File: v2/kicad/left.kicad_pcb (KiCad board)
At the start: 2 copper layers, 158.5 x 120.3 mm, 66 parts

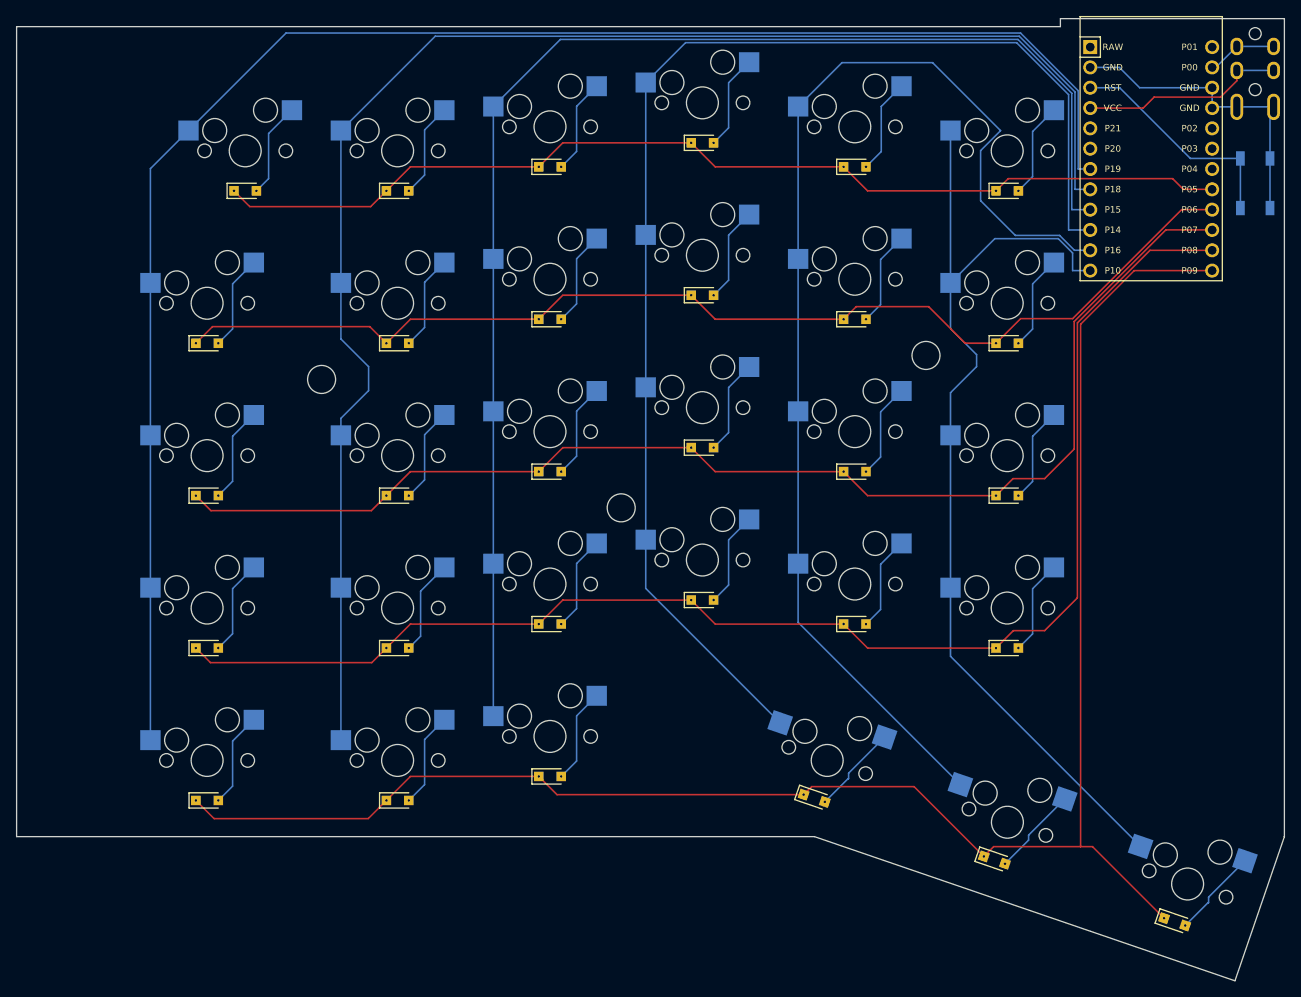
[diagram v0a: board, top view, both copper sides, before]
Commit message: Move backspace 1u to the left
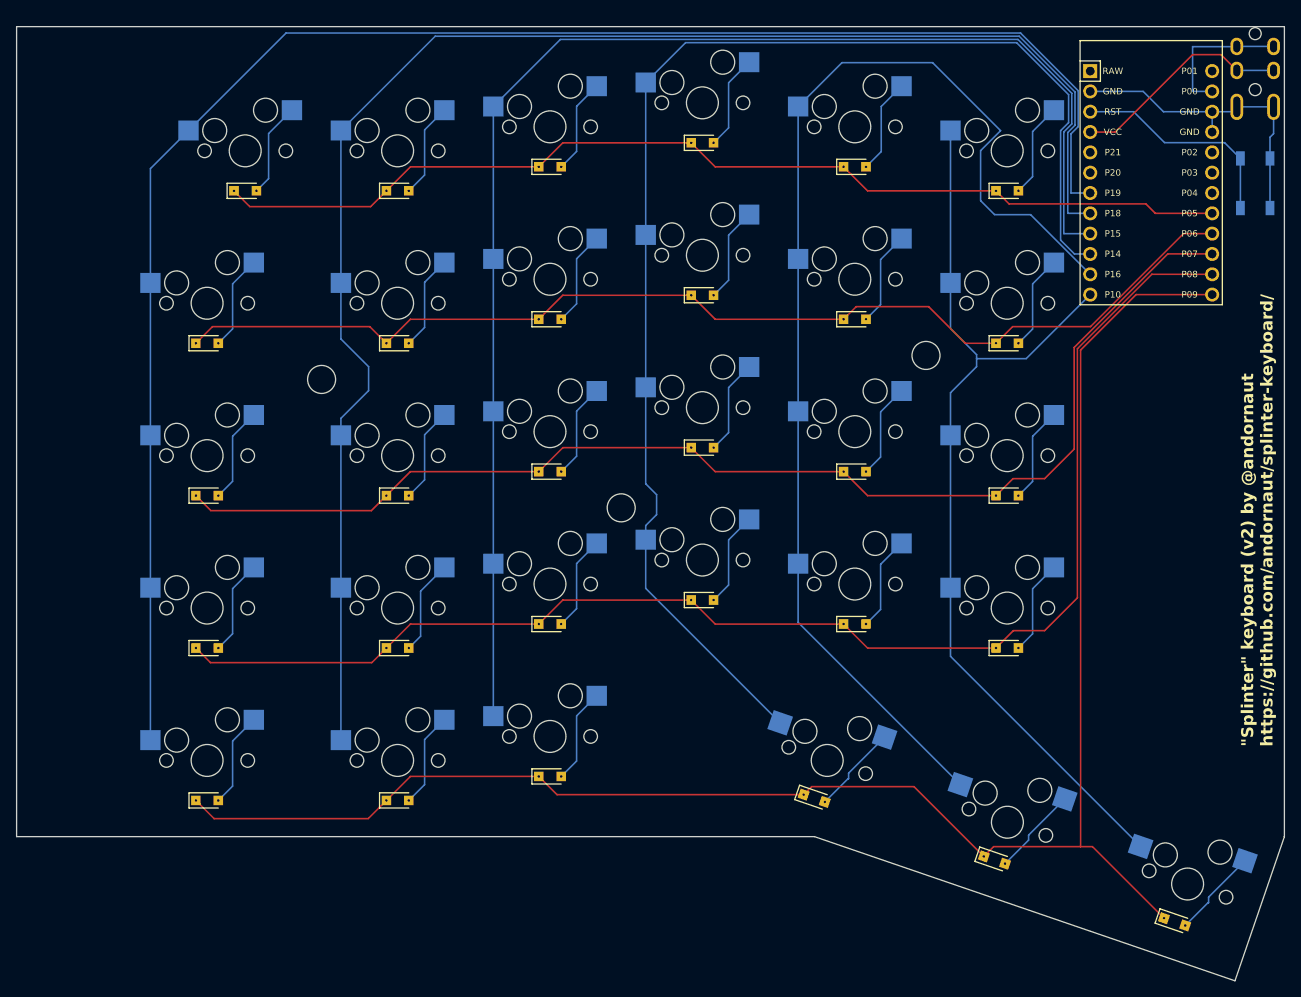
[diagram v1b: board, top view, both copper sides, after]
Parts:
- moved MCU1 3.00 mm to (181.8, 119.5)
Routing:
- net P0: track 7.65 -> 18.1 mm
- net P10: track 124.7 -> 119.5 mm
- net P14: track 164.2 -> 168.8 mm
- net P15: track 171.6 -> 176.0 mm
- net P18: track 192.7 -> 196.9 mm
- net P19: track 208.7 -> 213.0 mm
- net P7: track 156.6 -> 153.5 mm
- net P8: track 174.2 -> 171.1 mm
- net P9: track 217.9 -> 214.7 mm
- net VCC: track 25.6 -> 27.7 mm
- net P16: track 150.3 -> 151.6 mm
- net P6: track 141.9 -> 140.7 mm
- net RST: track 28.6 -> 27.4 mm
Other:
- board size 158.5 x 120.3 mm -> 158.5 x 119.3 mm
- board text added: "Pro Micro ATmega32U4 USB-C (3mm longer)"
- board text added: "Reset Switch"
- board text added: "TRRS"
- board text added: "{dblquote}Splinter{dblquote} keyboard (v2) by @andornaut https://github.com/andornaut/splinter-keyboard/"
